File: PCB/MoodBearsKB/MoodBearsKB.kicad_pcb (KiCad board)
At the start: 2 copper layers, 266.5 x 94.5 mm, 104 parts, among them J1 MJ-4PP-9, J2 MJ-4PP-9, U1 xiao-ble, U2 xiao-ble

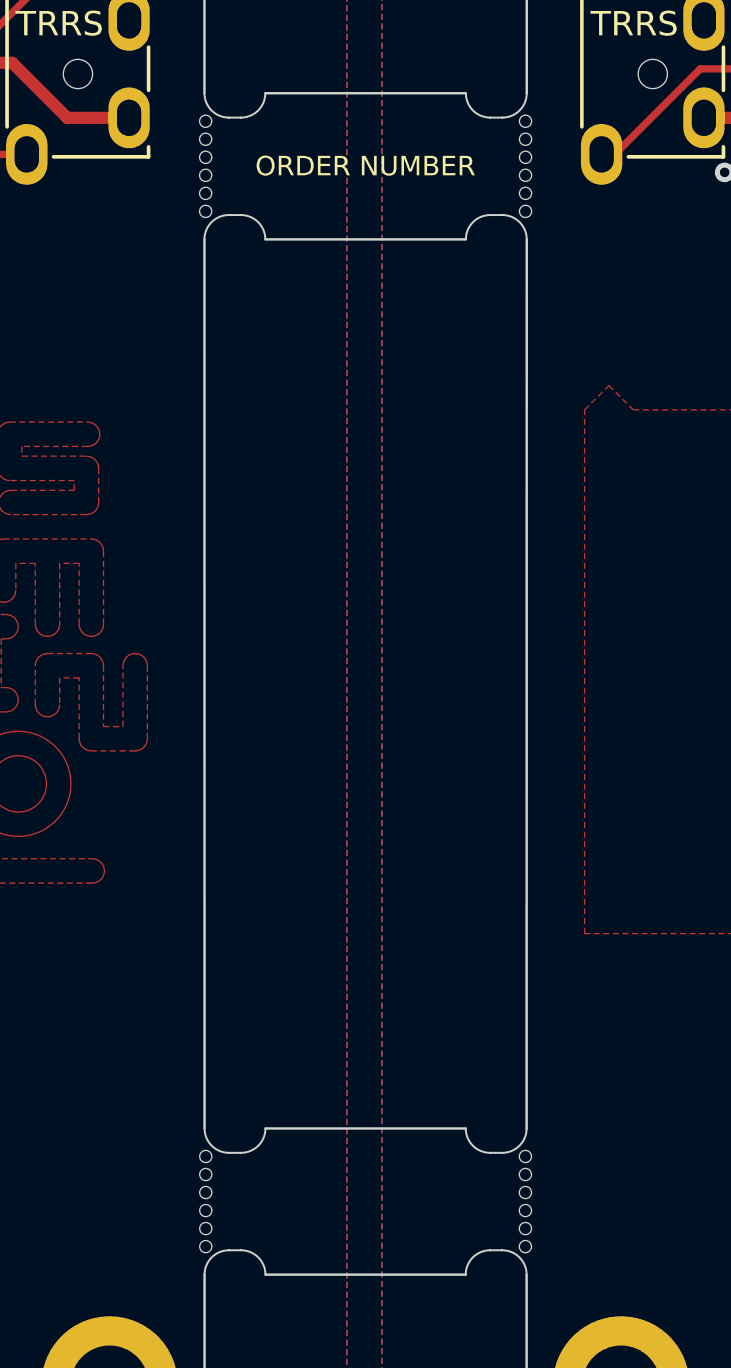
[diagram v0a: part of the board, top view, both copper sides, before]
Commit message: added documentation for schem and layout as pdf
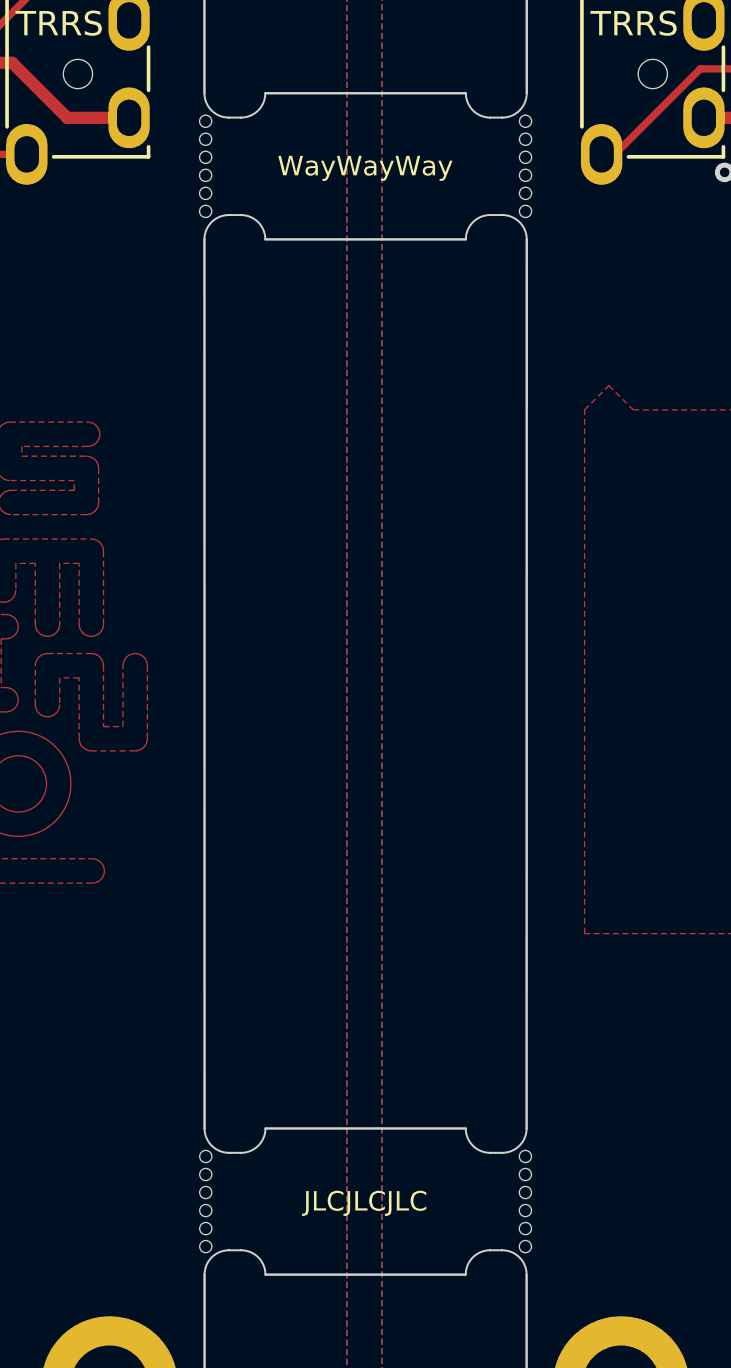
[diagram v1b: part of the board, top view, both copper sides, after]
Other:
- board text added: "JLCJLCJLC"
- board text added: "WayWayWay"
- board text removed: "ORDER NUMBER"
